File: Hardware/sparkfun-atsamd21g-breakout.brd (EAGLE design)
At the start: 17.8 x 33 mm, 41 parts, among them Q1 2N7002PW, Q3 2.5A/30V, U1 ATSAMD21G-A, U2 MIC5219 3.3V, U3 74AHC1G125, Y1 32.768kHz

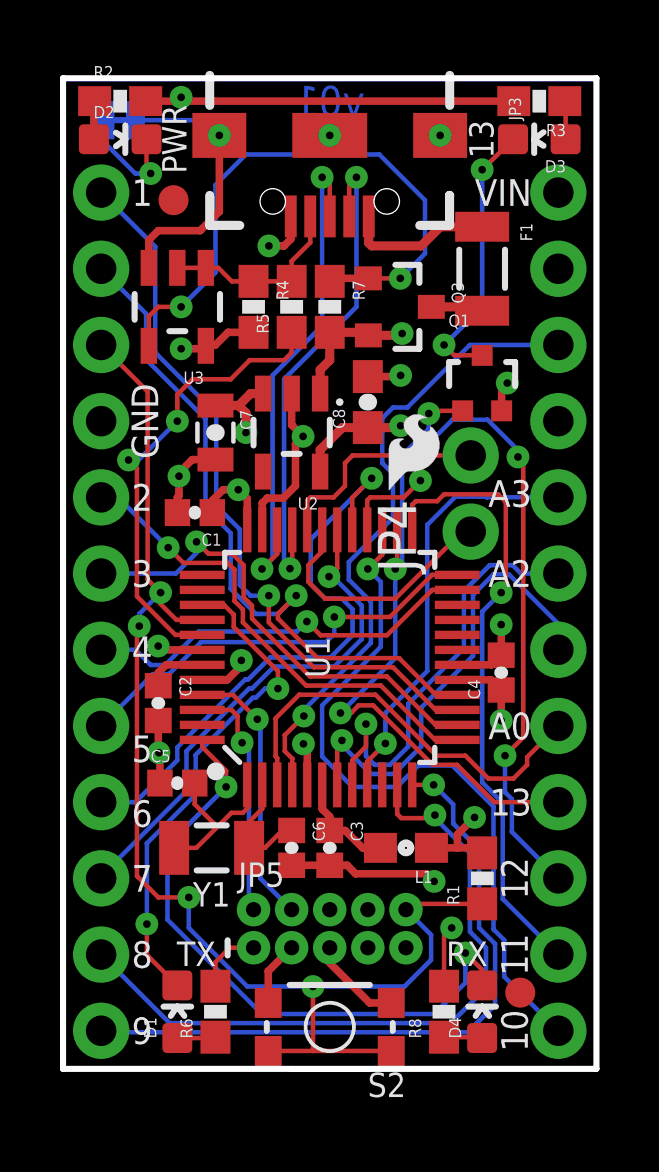
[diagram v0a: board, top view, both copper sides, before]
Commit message: Moving silk. Swapping D4 and D2.
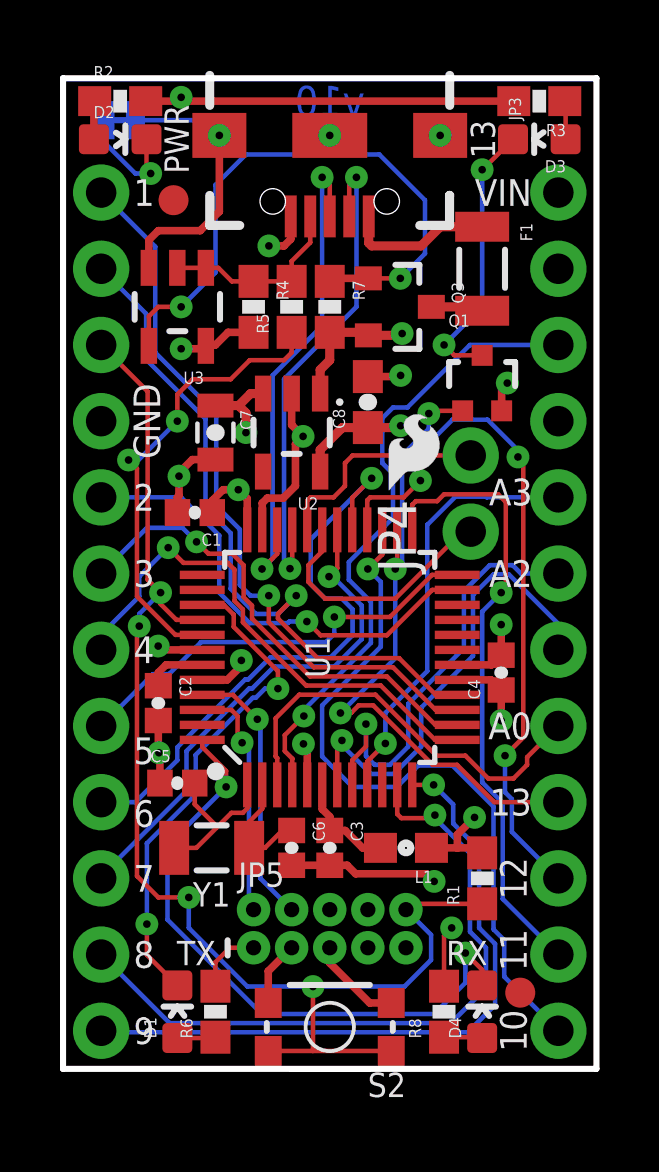
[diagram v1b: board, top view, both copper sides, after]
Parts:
- moved LOGO3 10.8 mm to (7.21, 5.94), turned to 90 degrees
- moved LOGO2 10.4 mm to (5.33, 17.6), turned to 90 degrees
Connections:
- net D2: now also U1.23; no longer U1.13
- net D4: now also U1.13; no longer U1.23
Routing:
- net D4: track 13.5 -> 17.5 mm
- net D2: track 16.1 -> 15.6 mm
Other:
- board text added: "v10"
- board text removed: "v01"

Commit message: Pulling buffer power up to RAW
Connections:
- net 3.3V: no longer R4.2, U3.5
- net RAW: now also R4.2, U3.5
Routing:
- net RAW: track 7.43 -> 10.4 mm, vias 2 -> 3
- net 3.3V: track 33.3 -> 30.6 mm, vias 8 -> 7
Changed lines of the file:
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@@
 <setting verticaltext="up"/>
 </settings>
-<grid distance="0.05" unitdist="inch" unit="inch" style="lines" multiple="1" display="yes" altdistance="0.001" altunitdist="inch" altunit="inch"/>
+<grid distance="0.05" unitdist="inch" unit="inch" style="lines" multiple="1" display="yes" altdistance="0.005" altunitdist="inch" altunit="inch"/>
 <layers>
-<layer number="1" name="Top" color="4" fill="1" visible="yes" active="yes"/>
-<layer number="2" name="Route2" color="11" fill="1" visible="no" active="yes"/>
+<layer number="1" name="Top" color="4" fill="1" visible="no" active="yes"/>
+<layer number="2" name="Route2" color="11" fill="1" visible="yes" active="yes"/>
 <layer number="3" name="Route3" color="4" fill="3" visible="no" active="no"/>
 <layer number="4" name="Route4" color="1" fill="4" visible="no" active="no"/>
@@
 <layer number="17" name="Pads" color="2" fill="1" visible="yes" active="yes"/>
 <layer number="18" name="Vias" color="2" fill="1" visible="yes" active="yes"/>
-<layer number="19" name="Unrouted" color="6" fill="1" visible="no" active="yes"/>
+<layer number="19" name="Unrouted" color="6" fill="1" visible="yes" active="yes"/>
 <layer number="20" name="Dimension" color="15" fill="1" visible="yes" active="yes"/>
-<layer number="21" name="tPlace" color="16" fill="1" visible="yes" active="yes"/>
-<layer number="22" name="bPlace" color="14" fill="1" visible="no" active="yes"/>
+<layer number="21" name="tPlace" color="16" fill="1" visible="no" active="yes"/>
+<layer number="22" name="bPlace" color="14" fill="1" visible="yes" active="yes"/>
 <layer number="23" name="tOrigins" color="15" fill="1" visible="yes" active="yes"/>
-<layer number="24" name="bOrigins" color="15" fill="1" visible="no" active="yes"/>
+<layer number="24" name="bOrigins" color="15" fill="1" visible="yes" active="yes"/>
 <layer number="25" name="tNames" color="7" fill="1" visible="no" active="yes"/>
 <layer number="26" name="bNames" color="7" fill="1" visible="no" active="yes"/>
@@
 <layer number="47" name="Measures" color="7" fill="1" visible="no" active="yes"/>
 <layer number="48" name="Document" color="7" fill="1" visible="no" active="yes"/>
-<layer number="49" name="Reference" color="7" fill="1" visible="no" active="yes"/>
+<layer number="49" name="Reference" color="7" fill="1" visible="yes" active="yes"/>
 <layer number="50" name="dxf" color="7" fill="1" visible="no" active="no"/>
 <layer number="51" name="tDocu" color="6" fill="1" visible="yes" active="yes"/>
@@
 <contactref element="R3" pad="2"/>
 <contactref element="JP5" pad="1"/>
-<contactref element="R4" pad="2"/>
-<contactref element="U3" pad="5"/>
 <via x="11.2522" y="21.4376" extent="1-16" drill="0.254"/>
 <wire x1="6.14" y1="17.966" x2="6.14" y2="19.006" width="0.254" layer="1"/>
@@
 <wire x1="14.605" y1="11.6078" x2="14.605" y2="12.628" width="0.254" layer="1"/>
 <wire x1="9.31" y1="21.375" x2="10.16" y2="21.375" width="0.3048" layer="1"/>
-<via x="3.937" y="24.003" extent="1-16" drill="0.254"/>
-<wire x1="4.76" y1="24.0999" x2="4.7901" y2="24.13" width="0.254" layer="1"/>
-<wire x1="4.7901" y1="24.13" x2="5.08" y2="24.13" width="0.254" layer="1"/>
-<wire x1="5.08" y1="24.13" x2="5.5" y2="24.55" width="0.254" layer="1"/>
-<wire x1="5.5" y1="24.55" x2="6.35" y2="24.55" width="0.254" layer="1"/>
-<wire x1="4.76" y1="24.0999" x2="4.6631" y2="24.003" width="0.254" layer="1"/>
-<wire x1="4.6631" y1="24.003" x2="3.937" y2="24.003" width="0.254" layer="1"/>
 <contactref element="R6" pad="2"/>
 <contactref element="R8" pad="2"/>
@@
 <wire x1="10.176" y1="24.45" x2="11.242" y2="24.45" width="0.3048" layer="1"/>
 <wire x1="11.242" y1="24.45" x2="11.303" y2="24.511" width="0.3048" layer="1"/>
+<contactref element="U3" pad="5"/>
+<contactref element="R4" pad="2"/>
+<via x="5.207" y="25.4" extent="1-16" drill="0.254"/>
+<wire x1="4.76" y1="24.0999" x2="4.76" y2="24.953" width="0.254" layer="1"/>
+<wire x1="4.76" y1="24.953" x2="5.207" y2="25.4" width="0.254" layer="1"/>
+<wire x1="5.207" y1="25.4" x2="5.5" y2="25.4" width="0.254" layer="1"/>
+<wire x1="5.5" y1="25.4" x2="6.35" y2="24.55" width="0.254" layer="1"/>
 </signal>
 <signal name="A3">
